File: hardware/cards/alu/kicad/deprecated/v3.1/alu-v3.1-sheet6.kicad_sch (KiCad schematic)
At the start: 7 parts, among them IC1 74*04, IC28 74*153, IC29 74*194, IC30 74*194, IC31 74*244, IC32 74*153, IC9 74*74

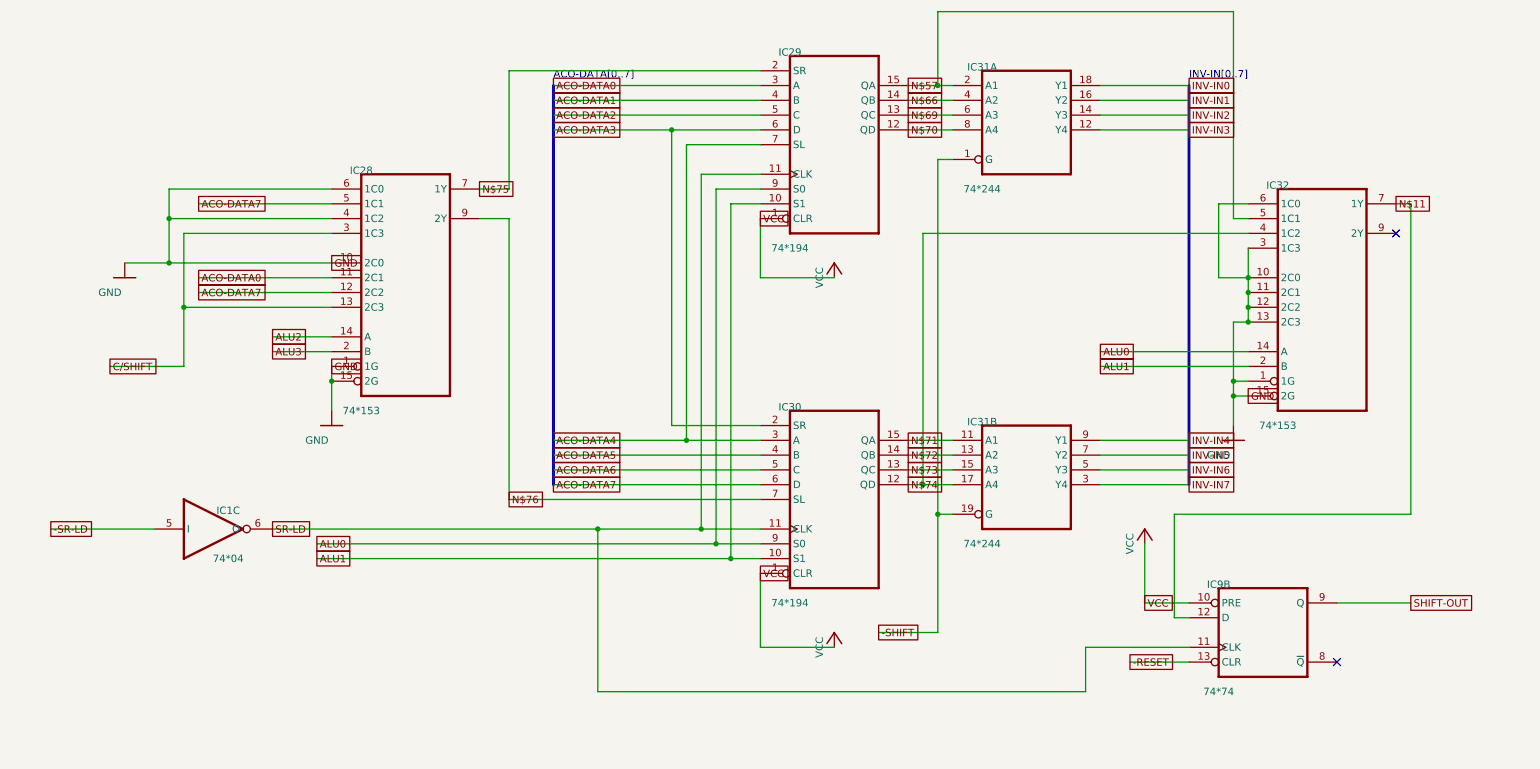
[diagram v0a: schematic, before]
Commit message: fix(kicad): readable converted schematics - overlaps 42,847 -> 3,147, nothing off the frame; CF sheet 0 overlaps
- tools/kicad/sch_overlaps.py: calibrated readability check (text/text, text/body, text/line, off frame/title block)
- eagle_sch_to_kicad.py: fields placed from Eagle's smashed attributes or the symbol's >NAME/>VALUE with Eagle's align,
  size and ratio, readable angles; fields Eagle never shows hidden (FABC96R shows only its pin name); pin numbers hidden
  where every Eagle pin hides them; Eagle-hidden layers dropped (the stray SpiceOrder text); labels on their own wires,
  converter labels only where KiCad needs them; rotate-then-mirror fixed for MR90/MR270 in pin_world/no-connects;
  each sheet on the smallest page that holds it, centred clear of the title block
- finish_board.py: stable footprint-library choice (DRC counts no longer vary run to run)
- all 37 projects regenerated: netlist proofs unchanged (34 MATCH, 2 schematic-only, video Fusion export MISMATCH as
  before); DRC same or better; ERC up (loose wire ends onto graphic buses no longer hidden by labels; explained per README)
- CF card: gate names off the gate bodies, U3 clear of its title, 5.08 mm connector pins; rebuilt: DRC 0/0, proof MATCH
- schematic PDFs regenerated (tools/sch_to_pdf.py, 37/37)

Co-Authored-By: Claude Opus 5.5 <noreply@anthropic.com>
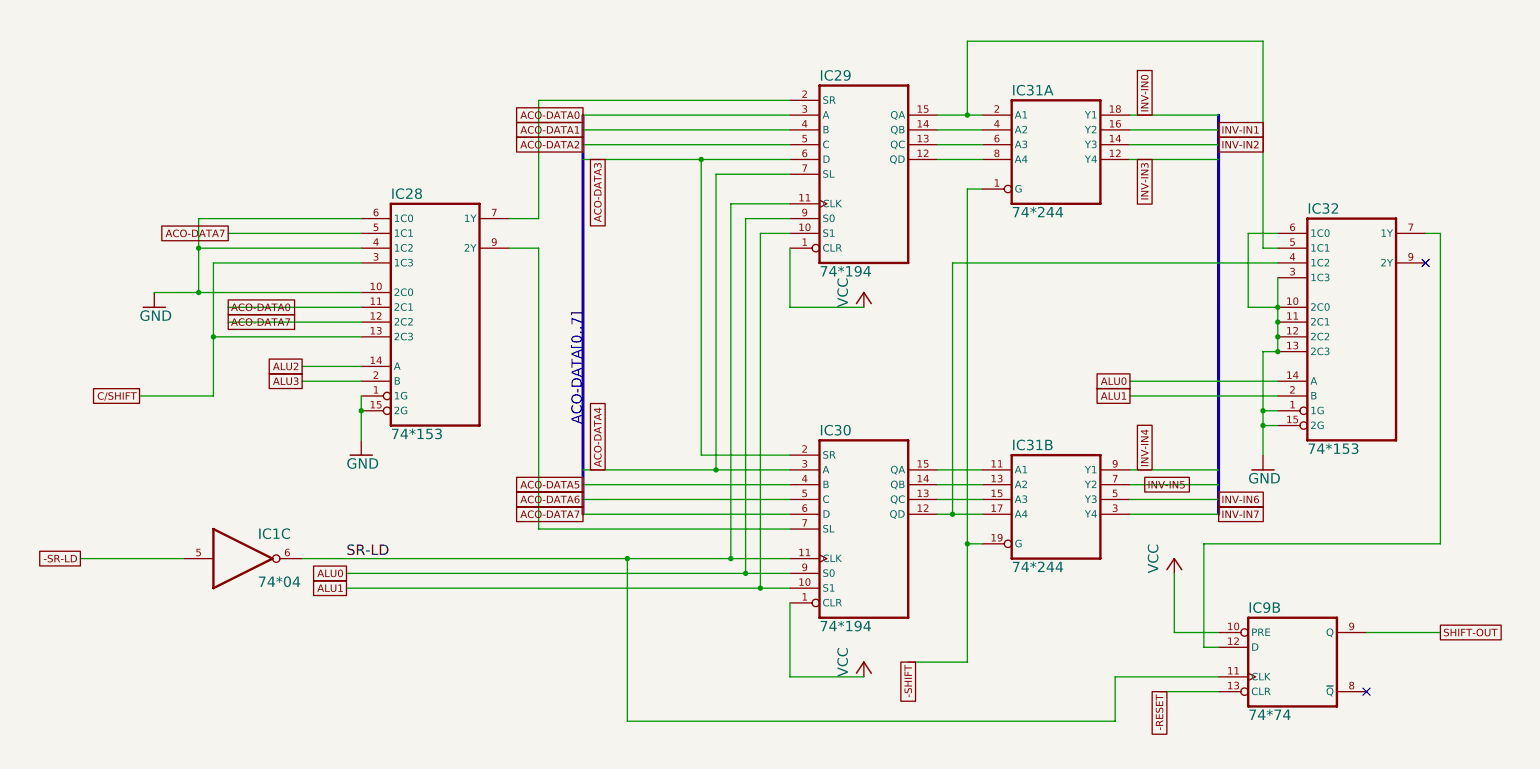
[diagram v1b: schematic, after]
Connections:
- net N$11: no longer names the net of IC32.7 (1Y), IC9.12 (D)
- net N$57: no longer names the net of IC29.15 (QA), IC31.2 (A1), IC32.5 (1C1)
- net N$66: no longer names the net of IC29.14 (QB), IC31.4 (A2)
- net N$69: no longer names the net of IC29.13 (QC), IC31.6 (A3)
- net N$70: no longer names the net of IC29.12 (QD), IC31.8 (A4)
- net N$71: no longer names the net of IC30.15 (QA), IC31.11 (A1)
- net N$72: no longer names the net of IC30.14 (QB), IC31.13 (A2)
- net N$73: no longer names the net of IC30.13 (QC), IC31.15 (A3)
- net N$74: no longer names the net of IC30.12 (QD), IC31.17 (A4), IC32.4 (1C2)
- net N$75: no longer names the net of IC28.7 (1Y), IC29.2 (SR)
- net N$76: no longer names the net of IC28.9 (2Y), IC30.7 (SL)
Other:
- note removed: "INV-IN[0..7]"
- moved on the sheet: IC28, IC29, IC30, IC31A, IC31B, IC32, IC9B
